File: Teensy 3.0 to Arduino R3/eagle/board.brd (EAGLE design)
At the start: 100 x 80 mm, 113 parts, among them IC1 78XX compatible, IC2 24AA256SN, IC3 24AA256SN, IC4 24AA256SN, IC5 24AA256SN, IC6 LTC2862, U1 MICROSD

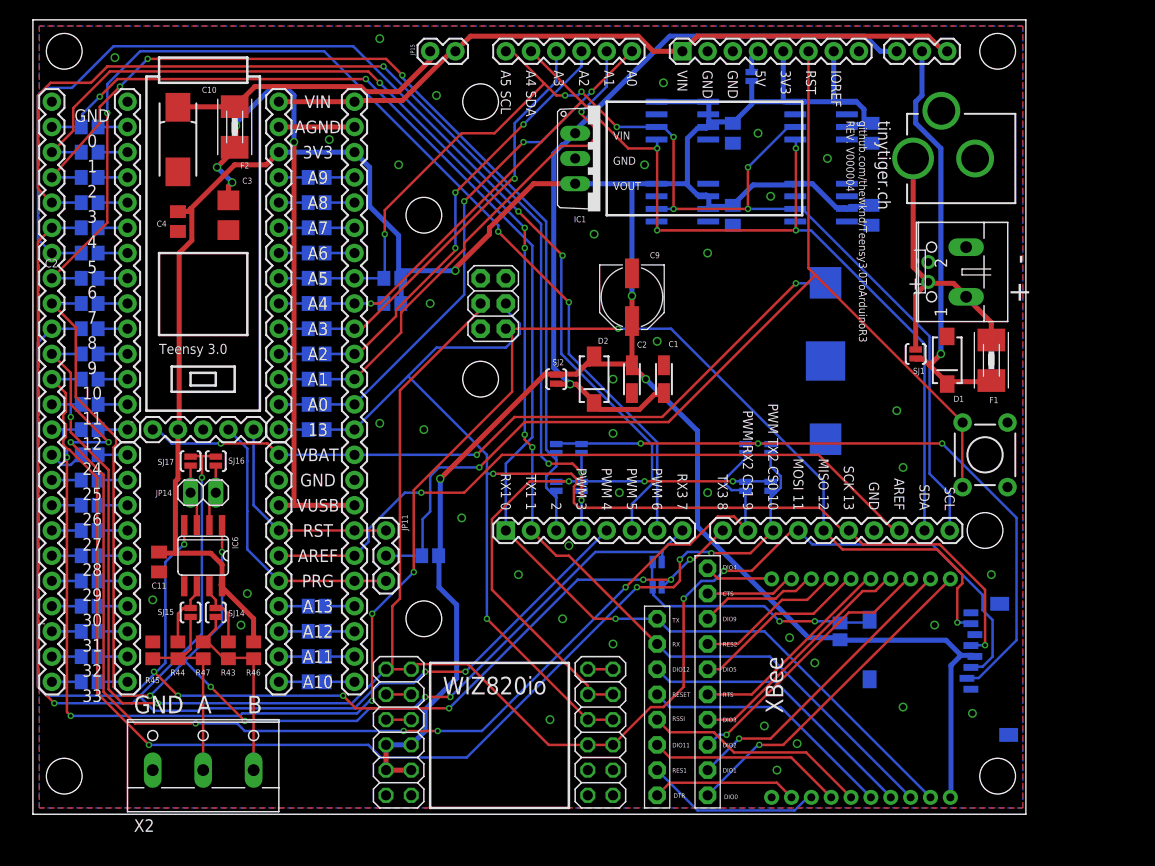
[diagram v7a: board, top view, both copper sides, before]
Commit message: added Li Battery Charger, variometer, temperature sensor
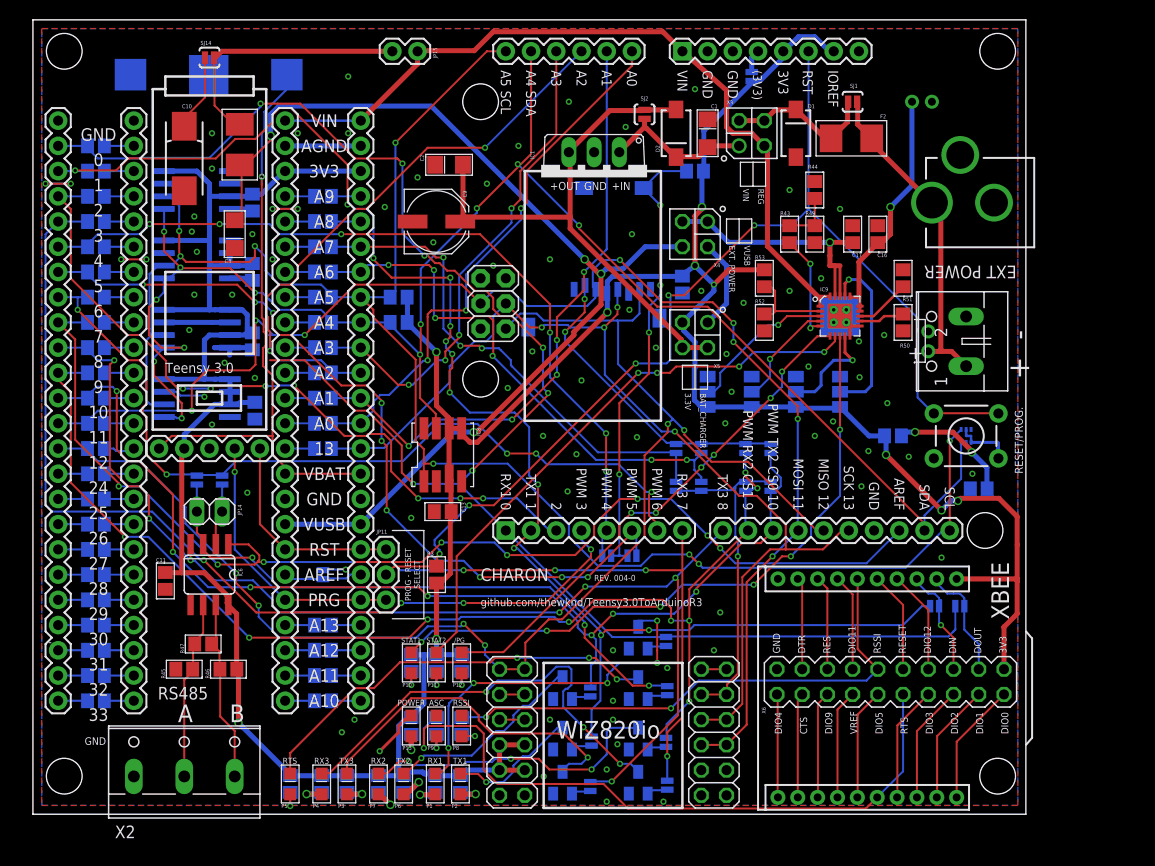
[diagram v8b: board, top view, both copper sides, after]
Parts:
- removed JP10: (no value), SparkFun-Connectors:1X03
- removed JP12: PINHD-1X10, adafruit:1X10-BIG
- removed JP13: (no value), adafruit:1X08-BIG
- added C12, C13, C16, C17: (no value), thewknd:0805C
- added CN3: (no value), adafruit:JST-PH-2-THM-RA
- added IC7: TMP102, thewknd:SOT563
- added IC8: MS5803-01BA, thewknd:MS5803
- added IC9: MCP73871, thewknd:QFN-20
- added P1, P13, P2, P3, P4, P5, P6, P7, P8, P9: LED, thewknd:LED0805
- added P10, P11, P12: (no value), thewknd:LED0805
- added Q1, Q2, Q3, Q4, Q5, Q6, Q7: 2N7002, adafruit:SOT23
- added R48, R49, R50, R51, R53, R54, R55, R56, R64, R65: (no value), thewknd:R0805
- added R52, R57, R58, R59, R60, R61, R62, R63, R66: RESISTOR, thewknd:R0805
- added SJ18, SJ19, SJ20, SJ25, SJ26, SJ27, SJ29, SJ30: (no value), SparkFun-Passives:SJ_2S-NO
- added SJ21, SJ22, SJ23, SJ24: (no value), SparkFun-Passives:SJ_2
- added SJ28: SOLDERJUMPERNO, SparkFun-Passives:SJ_2S-NO
- added X3, X4, X5: (no value), thewknd:HEADER-PTH-2X2
- added X6: HEADER-2X10SLK, thewknd:HEADER-PTH-2X10
- C1, C2: value (none) -> CAPACITOR_POL-3216-POL; device resistor:CT3216 -> thewknd:3216C-POL
- C11, C4, C5, C6, C7, C8: device rcl:C0805K -> thewknd:0805C
- C3: value (none) -> CAPACITOR_POL-3216-POL; device rcl:CT3528 -> thewknd:3216C-POL
- F1, F2: value (none) -> FUSE1812; device adafruit:1812 -> thewknd:1812STD
- IC2, IC3, IC4, IC5: value 24AA256SN -> 24AA1025SM; device microchip:SO-08 -> thewknd:SOIC-8
- R1, R10, R11, R12, R13, R14, R15, R16, R17, R18, R19, R2, R20, R21, R22, R23, R24, R25, R26, R27, R28, R29, R3, R30, R31, R32, R33, R34, R35, R36, R37, R38, R39, R40, R41, R42, R43, R44, R45, R46, R47, R5, R6, R7, R8, R9: device resistor:R0805 -> thewknd:R0805
- R4: value (none) -> R4; device resistor:R0805 -> thewknd:R0805
- moved R44 79.1 mm to (78.7, 62.9), turned to 90 degrees
- moved F1 78.7 mm to (20.8, 67.4), turned to 90 degrees
- moved R43 70.4 mm to (76.2, 58.4)
- moved BAT1 68.5 mm to (17.7, 74.5), turned to 0 degrees
- moved IC4 66.3 mm to (16.5, 48.9)
- moved C7 65.8 mm to (22.1, 47.6)
- moved IC2 62.9 mm to (16.5, 62.9)
- moved C5 62.4 mm to (22.1, 61.6)
- moved F2 62.1 mm to (82.4, 68.1), turned to 180 degrees
- moved IC5 56.3 mm to (16.5, 41.9)
- moved SJ14 55.9 mm to (17.8, 76.2), turned to 180 degrees
- moved C8 55.7 mm to (22.4, 40.6)
- moved C4 51.2 mm to (65.4, 53.3), flipped to the bottom
- moved IC3 49.2 mm to (16.5, 55.9)
- moved C6 48.7 mm to (22.1, 54.6)
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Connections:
- new net /PG: IC9.6, P12.C
- new net BAT_CHARGER: C17.1, IC9.18, IC9.19, X4.1, X4.3
- new net CE: IC9.17, SJ24.2
- new net DIO0: U$1.20, X6.2
- new net DIO1: U$1.19, X6.4
- new net DIO11: U$1.7, X6.13
- new net DIO12: U$1.4, X6.7
- new net DIO2: U$1.18, X6.6
- new net DIO3: U$1.17, X6.8
- new net DIO4: U$1.11, X6.20
- new net DIO5: U$1.15, X6.12
- new net DIO9: U$1.13, X6.16
- new net N$100: C16.1, CN3.1, IC9.14, IC9.15, IC9.16
- new net N$103: R43.1, R44.1, R49.1
- new net N$104: IC9.5, R43.2
- new net N$105: IC9.12, R50.1
- new net N$106: IC9.13, R51.1
- new net N$107: IC9.2, R52.1, R53.2
- new net N$109: C2.+, C9.+, D2.A, IC1.3, SJ2.1, X5.2, X5.4
- new net N$110: X4.2, X5.1
- new net N$111: P12.A, R54.2
- new net N$112: P11.A, R55.2
- new net N$113: P10.A, R56.2
- new net N$67: Q1.1, SJ20.1
- new net N$68: Q2.1, SJ25.2
- new net N$69: Q5.1, SJ28.1
- new net N$70: Q3.1, SJ26.1
- new net N$71: Q4.1, SJ27.2
- new net N$72: P8.A, R65.1
- new net N$73: P9.A, R64.1
- new net N$74: P13.A, R66.1
- new net PROG2: IC9.4, SJ22.2
- new net SEL: IC9.3, SJ21.2
- new net STAT1: IC9.8, P10.C
- new net STAT2: IC9.7, P11.C
- new net TE: IC9.9, SJ23.2
- new net VCC: C12.1, IC7.5, R48.1
- new net XBEE_CTS: U$1.12, X6.18
- new net XBEE_DIN: SJ30.2, U$1.3, X6.5
- new net XBEE_DOUT: SJ29.2, U$1.2, X6.3
- new net XBEE_DTR: U$1.9, X6.17
- new net XBEE_RES1: U$1.8, X6.15
- new net XBEE_RSSI: R65.2, U$1.6, X6.11
- new net XBEE_RST: U$1.5, X6.9
- new net XBEE_RTS: R64.2, U$1.16, X6.10
- new net XBEE_VREF: U$1.14, X6.14
- net 3.3V: now also C13.1, IC8.3, IC8.5, IC8.6, R48.2, R53.1, R54.1, R55.1, R56.1, R57.2, R58.2, R59.2, R60.2, R61.2, R62.2, R63.2, R66.2, SJ21.3, SJ22.3, SJ23.3, SJ24.3, X5.3, X6.1; no longer C2.+, C9.+, D2.A, IC1.3, SJ2.1
- net A4: now also IC7.6, IC8.7
- net A5: now also IC7.1, IC8.1
- net A6: now also SJ12.2, SJ8.2
- net A7: now also SJ11.2, SJ7.2
- net AREF: now also SJ15.2; no longer JP5.8
- net D0: now also SJ25.1, SJ29.1; no longer JP13.8, U$1.2
- net D1: now also SJ20.2, SJ30.1; no longer JP13.7, U$1.3
- net D10: now also SJ18.1
- net D11: no longer JP2.11, JP2.12
- net D12: now also JP2.11, JP2.12
- net D2: no longer SJ11.2, SJ7.2
- net D3: no longer SJ12.2, SJ8.2
- net D4: now also SJ3.2; no longer SJ16.1, SJ17.1
- net D5: now also SJ4.2
- net D6: now also SJ16.1, SJ17.1
- net D7: now also SJ26.2; no longer SJ3.2
- net D8: now also SJ27.1; no longer SJ4.2
- net D9: now also SJ19.1
- net EXT_POWER: now also F2.+; no longer F1.1
- net GND: now also C12.2, C13.2, C16.2, C17.2, CN3.2, IC7.2, IC7.4, IC8.2, IC9.10, IC9.11, IC9.21, IC9.22, IC9.P$1, IC9.P$2, IC9.P$3, IC9.P$4, P13.C, P8.C, P9.C, Q1.2, Q2.2, Q3.2, Q4.2, Q5.2, Q6.2, Q7.2, R44.2, R49.2, R50.2, R51.2, R52.2, SJ21.1, SJ22.1, SJ23.1, SJ24.1, X6.19
- net N$1: now also F2.-, X3.2, X3.4; no longer F1.2, JP10.2
- net N$2: now also F1.-, SJ14.1; no longer C10.+, F2.2
- net N$3: now also X3.1; no longer JP10.1
- net N$44: now also SJ28.2
- net N$45: now also P5.C, Q5.3; no longer JP13.6, U$1.4
- net N$46: now also P5.A, R57.1; no longer JP13.5, U$1.5
- net N$47: now also P4.A, R59.1; no longer JP13.4, U$1.6
- net N$48: now also P3.A, R58.1; no longer JP13.3, U$1.7
- net N$49: now also P3.C, Q4.3; no longer JP13.2, U$1.8
- net N$50: now also P4.C, Q3.3; no longer JP13.1, U$1.9
- net N$51: now also P1.A, R61.1; no longer JP12.1, U$1.20
- net N$54: now also P2.A, R60.1; no longer JP12.2, U$1.19
- net N$55: now also P1.C, Q2.3; no longer JP12.3, U$1.18
- net N$56: now also P2.C, Q1.3; no longer JP12.4, U$1.17
- net N$59: now also P7.A, R63.1; no longer JP12.5, U$1.16
- net N$60: now also P6.A, R62.1; no longer JP12.6, U$1.15
- net N$61: now also P6.C, Q7.3; no longer JP12.7, U$1.14
- net N$62: now also P7.C, Q6.3; no longer JP12.8, U$1.13
- net N$63: now also JP5.8, SJ15.1; no longer JP12.9, U$1.12
- net N$64: now also Q7.1, SJ18.2; no longer JP12.10, U$1.11
- net N$65: now also C10.+, SJ14.2; no longer IC6.7, R43.1, SJ14.1
- net N$66: now also Q6.1, SJ19.2; no longer IC6.6, R44.1, SJ15.1
- net RS485A: now also IC6.6; no longer R44.2, SJ15.2
- net RS485B: now also IC6.7; no longer R43.2, SJ14.2
- net VIN: now also IC9.1, IC9.20, X3.3; no longer JP10.3
- net VUSB: now also F1.+, X4.4; no longer F2.1
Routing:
- net XBEE_RTS: track 0.00 -> 69.4 mm, vias 0 -> 1
- net STAT1: track 0.00 -> 66.5 mm, vias 0 -> 6
- net D4: track 145.6 -> 82.0 mm, vias 4 -> 6
- net AREF: track 70.6 -> 8.00 mm, vias 1 -> 0
- net N$3: track 77.0 -> 15.7 mm, vias 1 -> 0
- net STAT2: track 0.00 -> 58.2 mm, vias 0 -> 4
- net N$63: track 9.06 -> 66.8 mm, vias 0 -> 6
- net N$109: track 0.00 -> 56.6 mm
- net D11: track 193.5 -> 139.0 mm, vias 4 -> 8
- net N$44: track 6.26 -> 60.4 mm, vias 0 -> 3
- net XBEE_RSSI: track 0.00 -> 53.9 mm, vias 0 -> 2
- net /PG: track 0.00 -> 51.9 mm, vias 0 -> 6
- net A5: track 126.1 -> 177.4 mm
- net GND: track 0.00 -> 50.7 mm, vias 40 -> 81
- net A6: track 2.96 -> 53.6 mm, vias 0 -> 6
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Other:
- board text added: "(3V3)"
- board text added: "+IN"
- board text added: "+OUT"
- board text added: "/PG"
- board text added: "3.3V"
- board text added: "4"
- board text added: "5"
- board text added: "A6"
- board text added: "A7"
- board text added: "ASC"
- board text added: "BAT"
- board text added: "BAT_CHARGER 3.3V"
- board text added: "CE"
- board text added: "CHARON"
- board text added: "DIO4 CTS DIO9 VREF DIO5 RTS DIO3 DIO2 DIO1 DIO0"
- board text added: "EXT POWER"
- board text added: "GND DTR RES DIO11 RSSI RESET DIO12 DIN DOUT 3V3"
- board text added: "I2C PULLUP"
- board text added: "MCP73871 CONFIGURATION"
- board text added: "POWER"
- board text added: "PROG - RESET SELECT"
- board text added: "PROG2"
- board text added: "REG VIN"
- board text added: "RESET/PROG."
- board text added: "REV. 004-0"
- board text added: "RS485"
- board text added: "RTC BAT"
- board text added: "RX1"
- board text added: "RX2"
- board text added: "RX3"
- board text added: "SD CARD DETECT"
- board text added: "SD SLAVE SELECT"
- board text added: "SEL"
- board text added: "STAT1"
- board text added: "STAT2"
- board text added: "TE"
- board text added: "TX1"
- board text added: "TX2"
- board text added: "TX3"
- board text added: "VUSB EXT. POWER"
- board text added: "WIZ820 SLAVE SELECT"
- board text added: "XBEE"
- board text removed: "5V"
- board text removed: "5V=3.3V"
- board text removed: "C2"
- board text removed: "CTS"
- board text removed: "D2"
- board text removed: "D3"
- board text removed: "DIO0"
- board text removed: "DIO1"
- board text removed: "DIO11"
- board text removed: "DIO12"
- board text removed: "DIO2"
- board text removed: "DIO3"
- board text removed: "DIO4"
- board text removed: "DIO5"
- board text removed: "DIO9"
- board text removed: "DTR"
- board text removed: "RES1"
- board text removed: "RES2"
- board text removed: "RESET"
- board text removed: "REV. V000004"
- board text removed: "RX"
- board text removed: "SD slave select"
- board text removed: "TX"
- board text removed: "VOUT"
- board text removed: "XBee"
- board text removed: "XBee slave select"
- board text removed: "tinytiger.ch"
